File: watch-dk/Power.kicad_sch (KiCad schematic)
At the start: 39 parts, among them IC401 nPM1300-QEXX, Q401 PMZ550UNEYL, Q402 PMZ550UNEYL, Q403 PMZ550UNEYL, Q404 PMZB320UPEYL, X401 Battery, X402 Battery, X403 Power

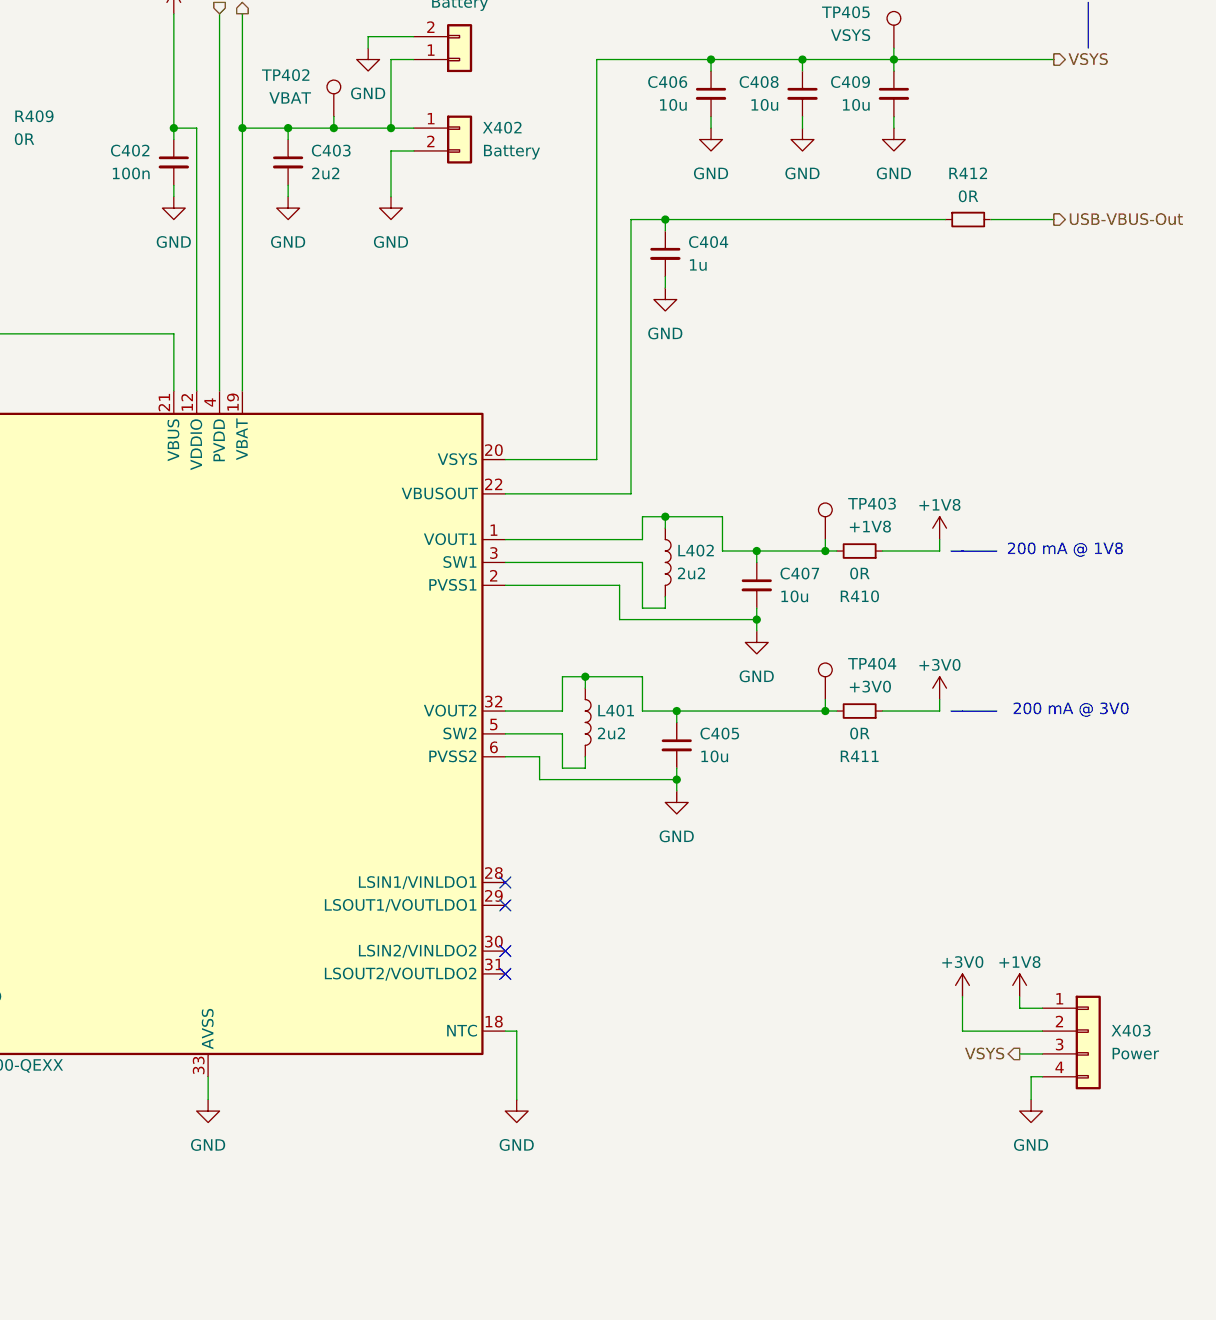
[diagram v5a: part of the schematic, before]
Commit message: Feature: Issue #145
- Update symbols

Signed-off-by: Daniel Kampert <DanielKampert@kampis-elektroecke.de>
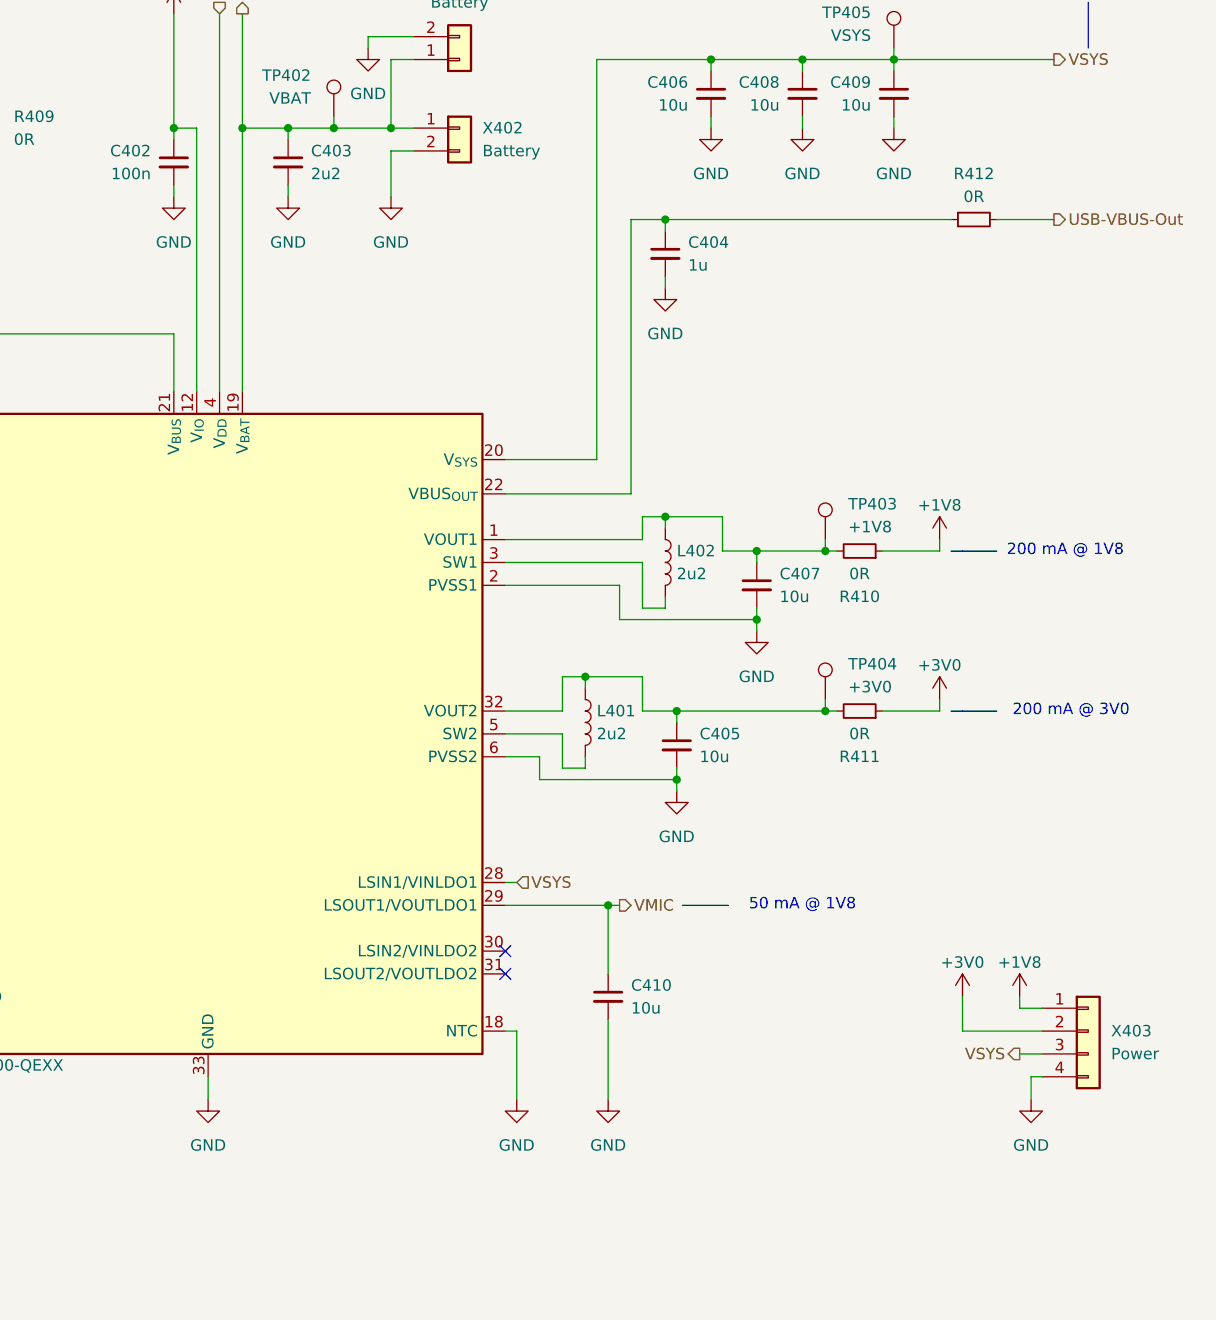
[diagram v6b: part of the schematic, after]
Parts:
- added C410: 10u, Capacitor_SMD:C_0402_1005Metric, symbol Device:C_Small
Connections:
- net GND: now also C410.2
- net VSYS: now also IC401.28 (LSIN1/VINLDO1)
- net VMIC: now reaches IC401.29 (LSOUT1/VOUTLDO1)
- net VMIC: now also C410.1
- no-connect marks 11 -> 9
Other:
- note added: "50 mA @ 1V8"
- moved on the sheet: R412
